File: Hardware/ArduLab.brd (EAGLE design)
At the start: 80 x 100 mm, 91 parts, among them CN1 USB-B, CN2 JST-PH, Q1 BSS138, Q2 BSS138, U1 ATMEGA32U4-AU, U2 MIC5205, U3 PAM2401, U4 MCP73831, U5 L293DD, X1 16MHz

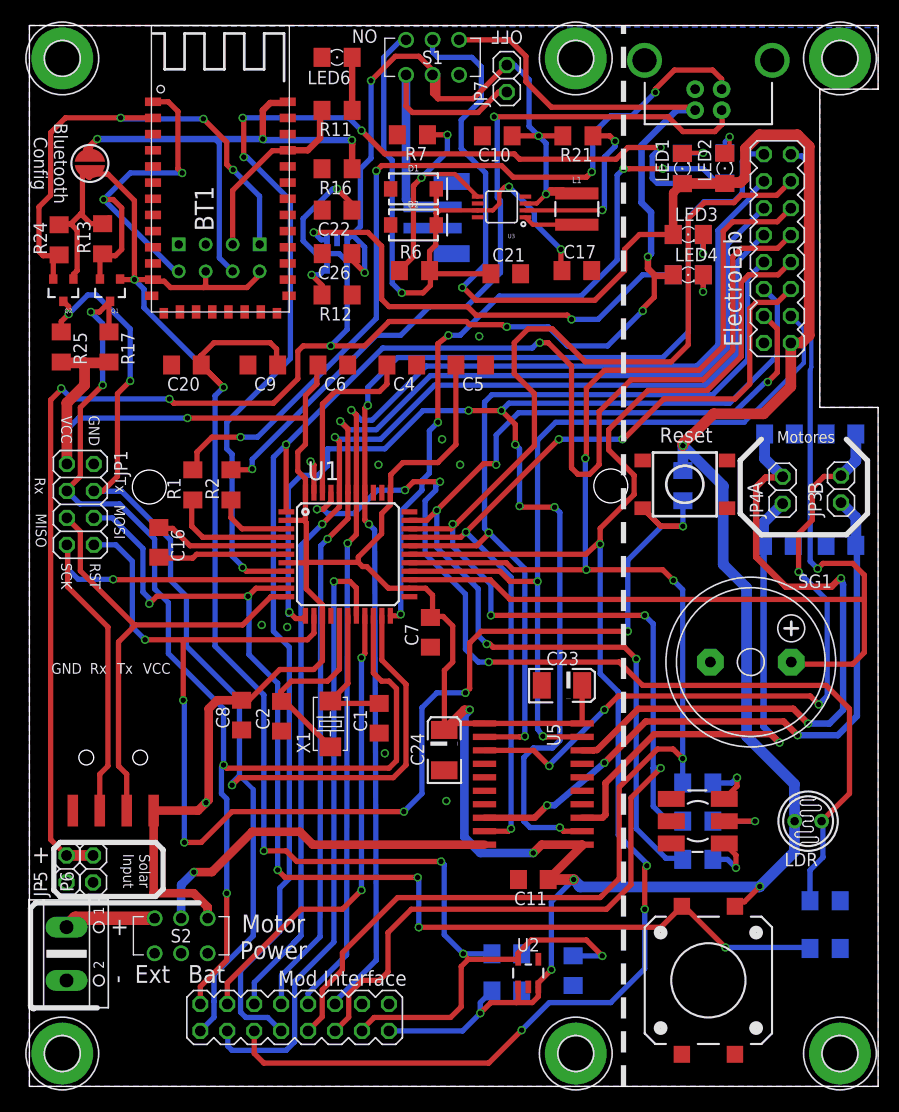
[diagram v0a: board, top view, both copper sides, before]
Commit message: SCH and BRD updated. Added Production files (GERBER, BOM and CENTROID)
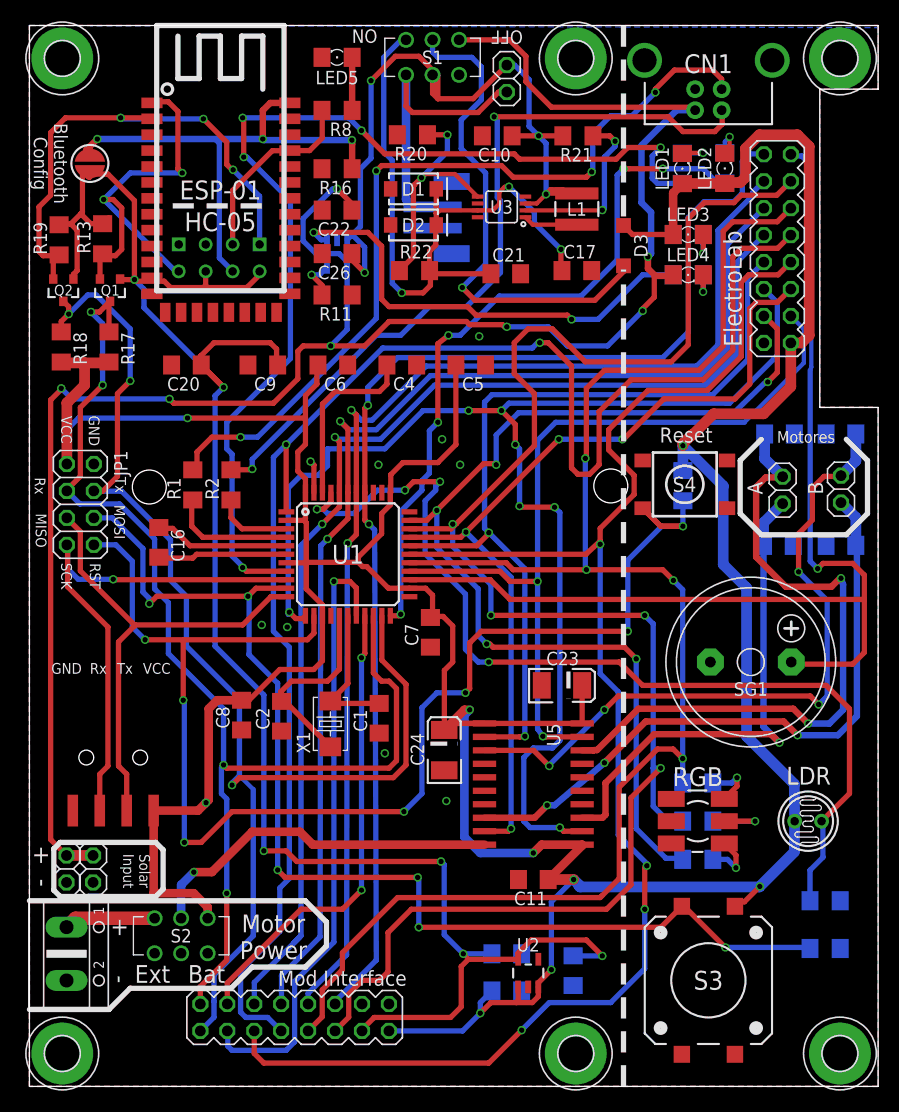
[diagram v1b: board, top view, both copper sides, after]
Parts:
- removed BT1: HC-05, Module:SERIAL_BLUETEETH
- removed R25: 10K, resistor:R1206
- added D3: MBR120, diode:SOD123
- added R22: 750K, resistor:R1206
- added U6: HC_05, Bluetooth HC-05:BLUETOOTH_SMD
- R11: value 1k -> 2k
- R12: value 2k -> 10K
- R20: value 470 -> 100k
- R6: value 750K -> 330
- R7: value 100k -> 470
- R8: value 330 -> 1k
- U1: device IC:TQFP44 -> adafruit:TQFP44
- moved R18 60.0 mm to (3.00, 69.7), flipped to the top, turned to 270 degrees
- moved R12 37.2 mm to (61.6, 56.6), flipped to the bottom, turned to 90 degrees
- moved R8 36.5 mm to (29.0, 92.0), flipped to the top
- moved R20 27.6 mm to (36.1, 89.7), flipped to the top
- moved R7 27.6 mm to (62.1, 80.3), flipped to the bottom
- moved R6 25.8 mm to (62.1, 76.5), flipped to the bottom, turned to 180 degrees
- moved R11 17.4 mm to (29.0, 74.6)
- renumbered LED6 to LED5, R24 to R19, S3 to PB1, S4 to PB2, X2 to CN3
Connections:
- new net N$3: D3.A, S1.5
- net 3.3V: now also U6.12; no longer BT1.12
- net CL: now also R8.2, U6.31; no longer BT1.31, R11.2
- net CONF: now also U6.34; no longer BT1.34
- net D1: now also R18.1; no longer R25.1
- net GND: now also R11.1, R20.2, R7.1, U6.13, U6.14, U6.21, U6.22; no longer BT1.13, BT1.14, BT1.21, BT1.22, R12.1, R20.1, R7.2
- net N$1: now also R20.1, R22.1; no longer R6.1, R7.1
- net N$10: now also R11.2; no longer R12.2
- net N$11: now also R6.1; no longer R8.1
- net N$14: now also R7.2; no longer R20.2
- net N$19: now also R8.1; no longer R11.1
- net N$9: now also R6.2; no longer R8.2
- net RST: now also R12.1; no longer R18.1
- net RX: now also U6.2; no longer BT1.2
- net TX: now also U6.1; no longer BT1.1
- net VCC: now also D3.C, R12.2; no longer R25.2, S1.5
- net VOUT: now also R22.2; no longer R6.2
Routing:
- net VCC: track 437.6 -> 388.8 mm, vias 10 -> 9
- net N$3: track 0.00 -> 47.1 mm, vias 0 -> 1
- net 3.3V: track 185.1 -> 186.1 mm
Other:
- board text added: "CN1"
- board text added: "ESP-01"
- board text added: "HC-05"
- board text added: "RGB"
- board text added: "S3"
- board text added: "S4"

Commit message: Update
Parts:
- renumbered PB1 to S3, PB2 to S4
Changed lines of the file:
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@@
 <setting verticaltext="up"/>
 </settings>
-<grid distance="1" unitdist="mm" unit="mm" style="lines" multiple="1" display="yes" altdistance="0.025" altunitdist="inch" altunit="inch"/>
+<grid distance="0.001" unitdist="inch" unit="inch" style="lines" multiple="1" display="yes" altdistance="0.025" altunitdist="inch" altunit="inch"/>
 <layers>
 <layer number="1" name="Top" color="4" fill="1" visible="yes" active="yes"/>
@@
 <element name="R12" library="resistor" package="R1206" value="10K" x="61.6" y="56.63" rot="MR90"/>
 <element name="U2" library="SparkFun" package="SOT23-5" value="MIC5205" x="47.02" y="10.68"/>
-<element name="PB2" library="Testing" package="TACTILE_SWITCH_TALL" value="Reset" x="61.78" y="56.75" rot="R180"/>
+<element name="S4" library="Testing" package="TACTILE_SWITCH_TALL" value="Reset" x="61.78" y="56.75" rot="R180"/>
 <element name="JP1" library="pinhead" package="2X04" value="" x="4.8" y="54.86" rot="R270"/>
 <element name="C16" library="resistor" package="C1206" value="1uF" x="12.2" y="51.28" rot="R270"/>
@@
 <element name="LED4" library="led" package="1206" value="Yellow" x="62.1" y="76.5"/>
 <element name="R6" library="resistor" package="R1206" value="330" x="62.1" y="76.5" rot="MR180"/>
-<element name="PB1" library="SparkFun-Electromechanical" package="TACTILE-SMD-12MM" value="B3FS-4052P" x="64" y="10" rot="R90"/>
+<element name="S3" library="SparkFun-Electromechanical" package="TACTILE-SMD-12MM" value="B3FS-4052P" x="64" y="10" rot="R90"/>
 <element name="C23" library="SparkFun" package="EIA3528-KIT" value="100uF" x="50.2" y="37.8"/>
 <element name="C11" library="resistor" package="C1206" value="100nF" x="47.5" y="19.5" rot="R180"/>
@@
 <signal name="GND">
 <contactref element="C3" pad="2"/>
-<contactref element="PB2" pad="A2"/>
+<contactref element="S4" pad="A2"/>
 <contactref element="U2" pad="2"/>
 <contactref element="JP1" pad="2"/>
@@
 <signal name="RST">
 <contactref element="R12" pad="1"/>
-<contactref element="PB2" pad="B2"/>
+<contactref element="S4" pad="B2"/>
 <contactref element="JP1" pad="8"/>
 <wire x1="6.07" y1="51.05" x2="8.15" y2="51.05" width="0.5" layer="16"/>
@@
 <contactref element="C11" pad="1"/>
 <contactref element="C24" pad="A"/>
-<contactref element="PB1" pad="1"/>
+<contactref element="S3" pad="1"/>
 <contactref element="U2" pad="1"/>
 <contactref element="U2" pad="3"/>
@@
 <signal name="D16">
 <contactref element="JP1" pad="6"/>
-<contactref element="PB1" pad="3"/>
+<contactref element="S3" pad="3"/>
 <contactref element="R15" pad="2"/>
 <wire x1="61.5" y1="16.975" x2="61.725" y2="16.975" width="0.5" layer="1"/>

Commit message: Updated
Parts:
- C22, C26: device resistor:C1206 -> resistor:C3216
- moved C17 7.20 mm to (44.9, 79.5), turned to 180 degrees
- moved C21 0.91 mm to (44.8, 75.7), turned to 180 degrees
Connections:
- net GND: now also C17.1, C21.1; no longer C17.2, C21.2
- net VOUT: now also C17.2, C21.2; no longer C17.1, C21.1
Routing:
- net VOUT: track 62.5 -> 52.8 mm, vias 3 -> 1
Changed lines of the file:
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@@
 <setting verticaltext="up"/>
 </settings>
-<grid distance="0.001" unitdist="inch" unit="inch" style="lines" multiple="1" display="yes" altdistance="0.025" altunitdist="inch" altunit="inch"/>
+<grid distance="0.1" unitdist="mm" unit="mm" style="lines" multiple="1" display="yes" altdistance="0.025" altunitdist="inch" altunit="inch"/>
 <layers>
 <layer number="1" name="Top" color="4" fill="1" visible="yes" active="yes"/>
@@
 <wire x1="7.5" y1="7.25" x2="0" y2="7.25" width="0.5" layer="25"/>
 <text x="61.75" y="56.75" size="1.4224" layer="25" align="center">S4</text>
+<wire x1="46.5" y1="34.8" x2="48.6" y2="34.8" width="0.4064" layer="25" curve="190.880664"/>
 </plain>
 <attributes>
@@
 </element>
 <element name="R11" library="resistor" package="R1206" value="2k" x="29" y="74.6" rot="R180"/>
-<element name="C22" library="resistor" package="C1206" value="4.7uF" x="29" y="82.6" rot="R180"/>
+<element name="C22" library="resistor" package="C3216" value="4.7uF" x="29" y="82.6" rot="R180"/>
 <element name="LED4" library="led" package="1206" value="Yellow" x="62.1" y="76.5"/>
 <element name="R6" library="resistor" package="R1206" value="330" x="62.1" y="76.5" rot="MR180"/>
@@
 <element name="R18" library="resistor" package="R1206" value="10K" x="3" y="69.7" rot="R270"/>
 <element name="U$1" library="esp8266modules" package="ESP01" value="ESP01" x="17.9" y="85"/>
-<element name="C26" library="resistor" package="C1206" value="4.7uF" x="29" y="78.5" rot="R180"/>
+<element name="C26" library="resistor" package="C3216" value="4.7uF" x="29" y="78.5" rot="R180"/>
 <element name="R22" library="resistor" package="R1206" value="750K" x="36.3" y="76.9"/>
 <element name="R20" library="resistor" package="R1206" value="100k" x="36.1" y="89.7" rot="R180"/>
@@
 </element>
 <element name="C10" library="resistor" package="C1206" value="22uF" x="44.1" y="89.6" rot="R180"/>
-<element name="C17" library="resistor" package="C1206" value="22uF" x="51.6" y="76.9"/>
-<element name="C21" library="resistor" package="C1206" value="22uF" x="44.9" y="76.6"/>
+<element name="C17" library="resistor" package="C1206" value="22uF" x="44.8802" y="79.4838" rot="R180"/>
+<element name="C21" library="resistor" package="C1206" value="22uF" x="44.8" y="75.7" rot="R180"/>
 <element name="LED3" library="led" package="1206" value="Green" x="62.1" y="80.3"/>
 <element name="SV2" library="con-lstb" package="MA08-2" value="" x="25" y="6.5">
@@
 <contactref element="R7" pad="1"/>
 <contactref element="C10" pad="2"/>
-<contactref element="C17" pad="2"/>
-<contactref element="C21" pad="2"/>
 <contactref element="D1" pad="A"/>
 <contactref element="D2" pad="A"/>
@@
 <contactref element="U1" pad="35"/>
 <contactref element="U1" pad="43"/>
+<contactref element="C17" pad="1"/>
+<contactref element="C21" pad="1"/>
 </signal>
 <signal name="AREF">
@@
 <contactref element="D1" pad="C"/>
 <contactref element="D2" pad="C"/>
-<contactref element="C17" pad="1"/>
-<contactref element="C21" pad="1"/>
 <wire x1="37.1" y1="74.8" x2="37.8" y2="75.5" width="0.5" layer="1"/>
 <wire x1="37.8" y1="75.5" x2="37.8" y2="76.822" width="0.5" layer="1"/>
 <wire x1="37.8" y1="76.822" x2="37.722" y2="76.9" width="0.5" layer="1"/>
-<wire x1="37.722" y1="76.9" x2="37.722" y2="78.722" width="0.5" layer="1"/>
-<wire x1="37.722" y1="78.722" x2="38.3" y2="79.3" width="0.5" layer="1"/>
-<wire x1="38.3" y1="79.3" x2="38.3" y2="81.15" width="0.5" layer="1"/>
-<wire x1="38.3" y1="81.15" x2="38.35" y2="81.2" width="0.5" layer="1"/>
-<wire x1="38.35" y1="81.2" x2="38.35" y2="82.3" width="0.5" layer="1"/>
-<wire x1="38.35" y1="82.3" x2="38.35" y2="84.6" width="0.5" layer="1"/>
-<wire x1="42.25" y1="82.575" x2="38.625" y2="82.575" width="0.4064" layer="1"/>
-<wire x1="38.625" y1="82.575" x2="38.35" y2="82.3" width="0.5" layer="1"/>
-<via x="50.1" y="78.9" extent="1-16" drill="0.5"/>
-<wire x1="50.1" y1="78.9" x2="50.1" y2="77" width="0.5" layer="1"/>
-<wire x1="50.1" y1="77" x2="50.2" y2="76.9" width="0.5" layer="1"/>
 <wire x1="35.5" y1="98.65" x2="35.05" y2="98.65" width="0.5" layer="16"/>
 <wire x1="35.05" y1="98.65" x2="33.4" y2="97" width="0.5" layer="16"/>
@@
 <via x="35.1" y="74.8" extent="1-16" drill="0.5"/>
 <wire x1="35.1" y1="74.8" x2="37.1" y2="74.8" width="0.5" layer="1"/>
-<wire x1="50.1" y1="78.9" x2="47.6" y2="81.4" width="0.5" layer="16"/>
-<wire x1="47.6" y1="81.4" x2="47.6" y2="82.4" width="0.5" layer="16"/>
-<wire x1="47.6" y1="82.4" x2="45.2" y2="84.8" width="0.5" layer="16"/>
-<via x="45.2" y="84.8" extent="1-16" drill="0.5"/>
-<wire x1="45.2" y1="84.8" x2="44.8" y2="84.8" width="0.4064" layer="1"/>
-<wire x1="44.8" y1="84.8" x2="44.3" y2="84.3" width="0.4064" layer="1"/>
-<wire x1="42.25" y1="82.575" x2="43.675" y2="82.575" width="0.4064" layer="1"/>
-<wire x1="43.675" y1="82.575" x2="44.3" y2="83.2" width="0.4064" layer="1"/>
-<wire x1="44.3" y1="83.2" x2="44.3" y2="84.3" width="0.4064" layer="1"/>
-<wire x1="43.5" y1="76.6" x2="38.022" y2="76.6" width="0.5" layer="1"/>
-<wire x1="38.022" y1="76.6" x2="37.722" y2="76.9" width="0.5" layer="1"/>
+<wire x1="42.25" y1="82.575" x2="41.1" y2="82.575" width="0.4064" layer="1"/>
+<wire x1="41.1" y1="82.575" x2="41.1" y2="82.6" width="0.4064" layer="1"/>
+<wire x1="41.1" y1="82.6" x2="40.7" y2="82.6" width="1.016" layer="1"/>
+<wire x1="40.7" y1="82.6" x2="38.35" y2="82.6" width="1.016" layer="1"/>
+<wire x1="38.35" y1="82.6" x2="38.35" y2="81.2" width="1.016" layer="1"/>
+<wire x1="38.35" y1="84.6" x2="38.35" y2="82.6" width="1.016" layer="1"/>
+<wire x1="40.7" y1="76.9" x2="40.7" y2="79.4838" width="1.016" layer="1"/>
+<wire x1="40.7" y1="79.9" x2="40.7" y2="82.6" width="1.016" layer="1"/>
+<wire x1="37.722" y1="76.9" x2="40.7" y2="76.9" width="1.016" layer="1"/>
+<contactref element="C17" pad="2"/>
+<contactref element="C21" pad="2"/>
+<wire x1="43.4" y1="75.7" x2="43.4802" y2="75.7" width="1.016" layer="1"/>
+<wire x1="43.4802" y1="75.7" x2="43.4802" y2="79.4838" width="1.016" layer="1"/>
+<wire x1="43.4802" y1="79.4838" x2="40.7" y2="79.4838" width="1.016" layer="1"/>
+<wire x1="40.7" y1="79.4838" x2="40.7" y2="79.9" width="1.016" layer="1"/>
 </signal>
 <signal name="N$10">

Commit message: Added drill hole for battery holding.
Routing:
- net A1: track 114.8 -> 119.6 mm
- net D6: track 149.0 -> 150.2 mm
- net VCC: track 388.8 -> 388.6 mm, vias 9 -> 8
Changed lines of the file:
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@@
 <text x="61.75" y="56.75" size="1.4224" layer="25" align="center">S4</text>
 <wire x1="46.5" y1="34.8" x2="48.6" y2="34.8" width="0.4064" layer="25" curve="190.880664"/>
+<hole x="33" y="15" drill="3.2"/>
 </plain>
 <attributes>
@@
 <wire x1="17.7" y1="36.4" x2="16.9" y2="35.6" width="0.8128" layer="1"/>
 <wire x1="16.9" y1="35.6" x2="16.9" y2="27" width="0.8128" layer="1"/>
-<wire x1="16.65" y1="26.75" x2="15.9" y2="26" width="0.8128" layer="1"/>
+<wire x1="16.9" y1="27" x2="15.9" y2="26" width="0.8128" layer="1"/>
 <wire x1="15.9" y1="26" x2="11.71" y2="26" width="0.8128" layer="1"/>
-<wire x1="16.5" y1="26.6" x2="16.65" y2="26.75" width="0.8128" layer="16"/>
-<via x="16.65" y="26.75" extent="1-16" drill="0.5"/>
-<wire x1="16.65" y1="26.75" x2="16.9" y2="27" width="0.8128" layer="1"/>
 <wire x1="47.97" y1="9.3799" x2="47.97" y2="9.77" width="0.5" layer="1"/>
 <wire x1="47.97" y1="9.77" x2="49.2" y2="11" width="0.5" layer="1"/>
@@
 <wire x1="67.9" y1="87.9" x2="69.19" y2="87.9" width="0.5" layer="16"/>
 <wire x1="69.19" y1="87.9" x2="69.23" y2="87.86" width="0.4064" layer="16"/>
-<wire x1="32.54" y1="52.46" x2="32.7" y2="11.9" width="0.5" layer="16"/>
-<wire x1="32.7" y1="11.9" x2="28.84" y2="8.04" width="0.5" layer="16"/>
-<wire x1="28.84" y1="8.04" x2="28.84" y2="7.8" width="0.5" layer="16"/>
 <contactref element="SV2" pad="12"/>
 <wire x1="28.84" y1="7.8" x2="28.81" y2="7.77" width="0.5" layer="16"/>
 <contactref element="U1" pad="37"/>
+<wire x1="28.84" y1="7.8" x2="28.84" y2="8.64" width="0.5" layer="16"/>
+<wire x1="28.84" y1="8.64" x2="30.8" y2="10.6" width="0.5" layer="16"/>
+<wire x1="30.8" y1="10.6" x2="33.5" y2="10.6" width="0.5" layer="16"/>
+<wire x1="33.5" y1="10.6" x2="35.6" y2="12.7" width="0.5" layer="16"/>
+<wire x1="35.6" y1="12.7" x2="35.6" y2="17.1" width="0.5" layer="16"/>
+<wire x1="35.6" y1="17.1" x2="32.7" y2="20" width="0.5" layer="16"/>
+<wire x1="32.7" y1="20" x2="32.7" y2="52.3" width="0.5" layer="16"/>
+<wire x1="32.7" y1="52.3" x2="32" y2="53" width="0.5" layer="16"/>
 </signal>
 <signal name="A0">
@@
 <wire x1="27.6" y1="6.56" x2="27.6" y2="9.1" width="0.5" layer="1"/>
 <wire x1="27.6" y1="9.1" x2="29.5" y2="11" width="0.5" layer="1"/>
-<wire x1="53.95" y1="17.95" x2="55.6" y2="19.6" width="0.5" layer="1"/>
+<wire x1="53.8" y1="17.8" x2="55.6" y2="19.6" width="0.5" layer="1"/>
 <wire x1="55.6" y1="19.6" x2="55.6" y2="28.2" width="0.5" layer="1"/>
 <wire x1="63.1" y1="67.5" x2="54.2" y2="67.5" width="0.5" layer="1"/>
@@
 <contactref element="SV2" pad="9"/>
 <wire x1="27.6" y1="6.56" x2="26.27" y2="5.23" width="0.5" layer="1"/>
-<wire x1="29.5" y1="11" x2="29.5" y2="12.6" width="0.5" layer="1"/>
-<wire x1="29.5" y1="12.6" x2="34.7" y2="17.8" width="0.5" layer="1"/>
-<wire x1="34.7" y1="17.8" x2="53.8" y2="17.8" width="0.5" layer="1"/>
-<wire x1="53.8" y1="17.8" x2="53.95" y2="17.95" width="0.5" layer="1"/>
 <contactref element="U1" pad="27"/>
+<wire x1="29.5" y1="11" x2="29.5" y2="14.7" width="0.5" layer="1"/>
+<wire x1="29.5" y1="14.7" x2="32.6" y2="17.8" width="0.5" layer="1"/>
+<wire x1="32.6" y1="17.8" x2="53.8" y2="17.8" width="0.5" layer="1"/>
 </signal>
 <signal name="D7">
@@
 <wire x1="30.1" y1="8.7" x2="31.4" y2="10" width="0.5" layer="1"/>
 <wire x1="31.4" y1="10" x2="33" y2="10" width="0.5" layer="1"/>
-<wire x1="33" y1="10" x2="33.8" y2="10.8" width="0.5" layer="1"/>
-<wire x1="33.8" y1="10.8" x2="33.8" y2="14.5" width="0.5" layer="1"/>
-<wire x1="33.8" y1="14.5" x2="36" y2="16.7" width="0.5" layer="1"/>
-<wire x1="36" y1="16.7" x2="54.4" y2="16.7" width="0.5" layer="1"/>
 <wire x1="54.4" y1="16.7" x2="56.7" y2="19" width="0.5" layer="1"/>
 <wire x1="56.7" y1="19" x2="56.7" y2="27.2" width="0.5" layer="1"/>
@@
 <wire x1="30.1" y1="6.52" x2="28.81" y2="5.23" width="0.5" layer="1"/>
 <contactref element="U1" pad="31"/>
+<wire x1="54.4" y1="16.7" x2="36.6" y2="16.7" width="0.5" layer="1"/>
+<wire x1="36.6" y1="16.7" x2="35.6" y2="15.7" width="0.5" layer="1"/>
+<wire x1="35.6" y1="15.7" x2="35.6" y2="12.6" width="0.5" layer="1"/>
+<wire x1="35.6" y1="12.6" x2="33" y2="10" width="0.5" layer="1"/>
 </signal>
 <signal name="N$6">
